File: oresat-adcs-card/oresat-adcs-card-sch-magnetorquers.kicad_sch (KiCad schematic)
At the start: 67 parts

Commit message: Design review changes
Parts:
- added R129: CRGCQ0603F2K7, oresat-acs-card:.0603-C-NOSILK, symbol oresat-acs-card-eagle-import:R-US_0603-C-NOSILK
- C17, C5, C53, C65, C66, C77: value (none) -> 10n; footprint (none) -> Capacitor_SMD:C_0603_1608Metric
- C18, C55, C67: value (none) -> 1n; footprint (none) -> Capacitor_SMD:C_0603_1608Metric
- C19, C56, C68: value (none) -> 22n; footprint (none) -> Capacitor_SMD:C_0603_1608Metric
- C26, C58, C70: value (none) -> 22u; footprint (none) -> Capacitor_SMD:C_0603_1608Metric
- C27, C40, C59, C61, C71, C73: value (none) -> NP; footprint (none) -> Capacitor_SMD:C_0603_1608Metric
- C41, C42, C62: value (none) -> 100n; footprint (none) -> Capacitor_SMD:C_0603_1608Metric
- C51, C54, C63: value (none) -> 4.7u; footprint (none) -> Capacitor_SMD:C_0603_1608Metric
- C52, C60, C72: value (none) -> 2.2u; footprint (none) -> Capacitor_SMD:C_0603_1608Metric
- R15, R16, R25: value (none) -> 30m; footprint (none) -> oresat-acs-card:WSK1206
- R17, R21, R23, R29: value (none) -> 1k; footprint (none) -> Resistor_SMD:R_0603_1608Metric
- R18, R24, R30: value (none) -> 47k; footprint (none) -> Resistor_SMD:R_0603_1608Metric
- R20: value (none) -> 100k; footprint (none) -> Resistor_SMD:R_0603_1608Metric
- R22: value (none) -> 18k; footprint (none) -> oresat-acs-card:.0603-C-NOSILK
- TP20, TP46, TP47, TP48, TP50, TP52, TP53, TP54, TP55, TP57, TP58, TP60, TP77, TP78, TP79, TP80, TP81, TP83, TP84: value (none) -> TEST-POINT-LARGE-SQUARE; footprint (none) -> oresat-acs-card:1X01
- U16, U22, U3: value (none) -> STSPIN250; footprint (none) -> Package_DFN_QFN:VQFN-16-1EP_3x3mm_P0.5mm_EP1.8x1.8mm
- U21, U23, U4: value (none) -> INA185; footprint (none) -> Package_TO_SOT_SMD:SOT-563
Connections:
- net GND: now also R129.1
- net MT_EN: now also R129.2
- net MT_REF: now reaches C5.1, C53.1, C65.1, R20.1, R21.2, TP20.1, U16.11 (REF), U22.11 (REF), U3.11 (REF)
- net MT_FAULT renamed MT_EN/~{FAULT}
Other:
- note added: "From MCU"
- note added: "MT_EN/~{FAULT}"
- note added: "STSPIN pulls EN/~{FAULT} low during failure disabling the magnetorquers"
- note added: "using 100x gain amp max 1 A out 1A*Rsense*100 = 3.0 V => 30 mΩ 30 mW"
- note removed: "30 mW max"
- note removed: "using 100x gain amp max 1 A out 1A*Rsense*100 = 3.0 V => 30 mΩ"
- moved on the sheet: C17, C18, C19, C26, C27, C40, C41, C5, C51, C52, R15, R17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

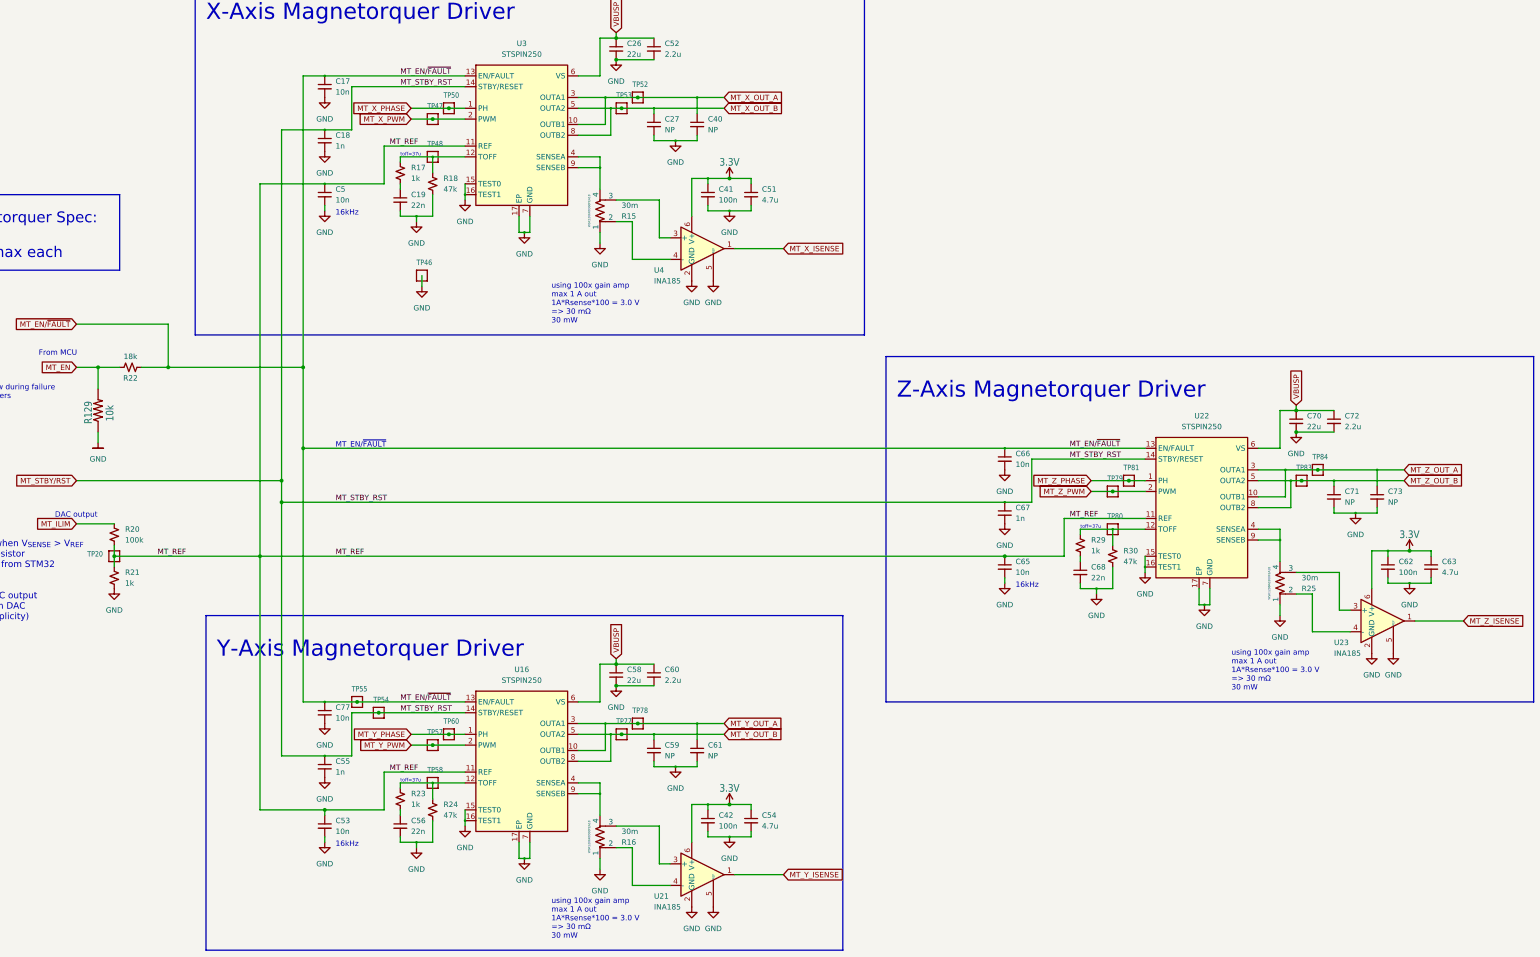
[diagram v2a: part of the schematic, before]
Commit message: Fixed ADCS card issues
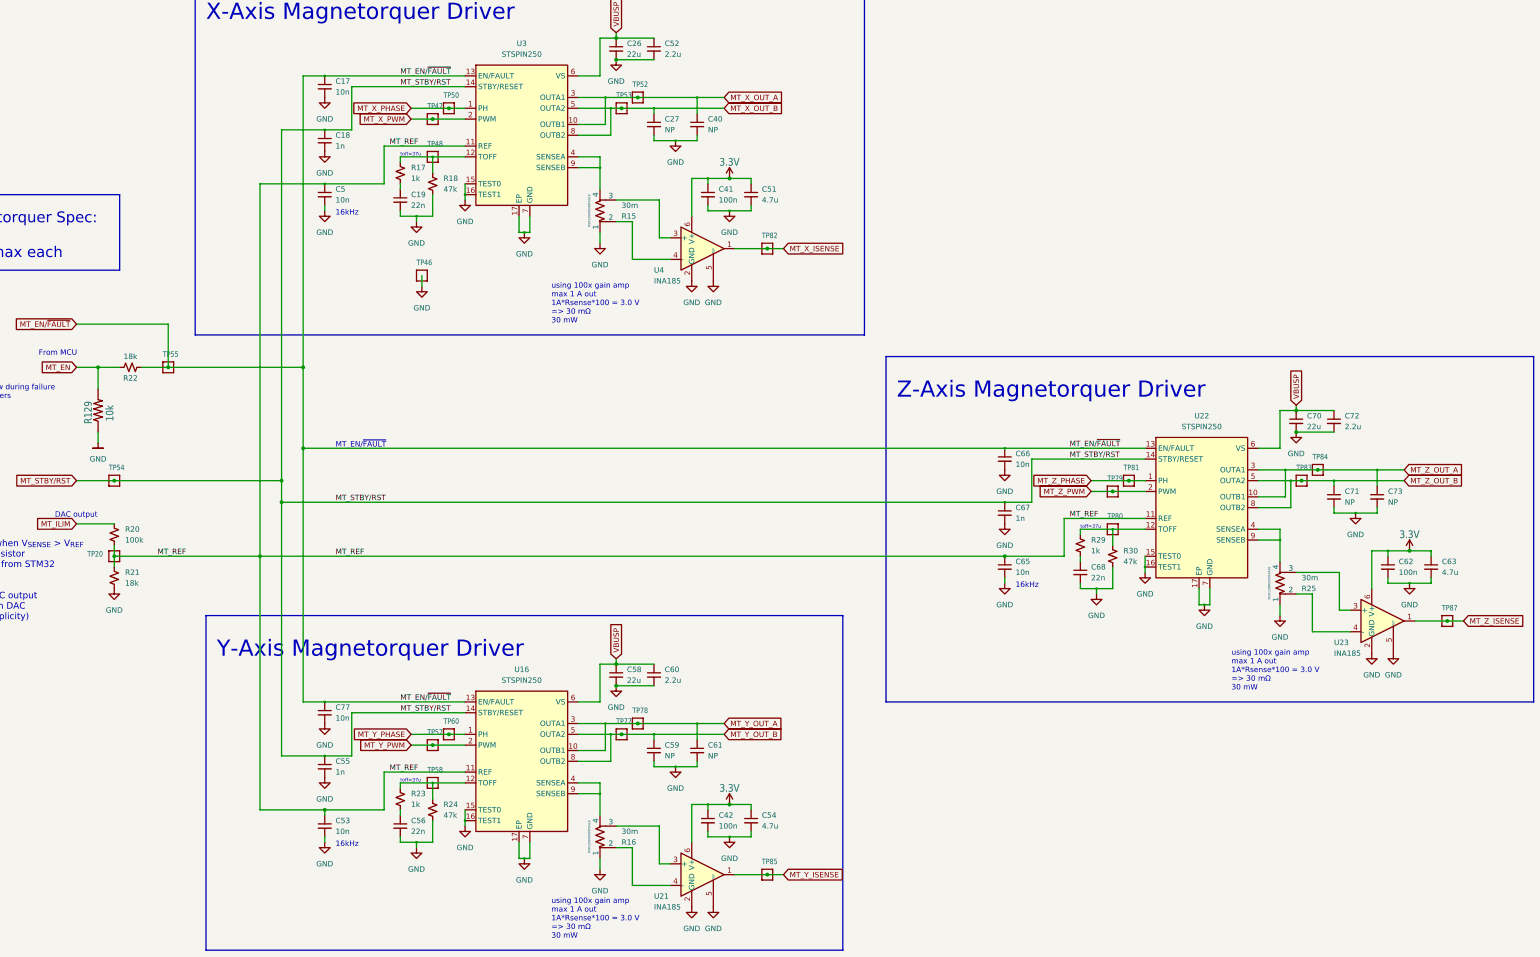
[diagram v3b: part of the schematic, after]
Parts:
- added TP82, TP85, TP87: TEST-POINT-LARGE-SQUARE, oresat-acs-card:1X01, symbol oresat-acs-card-eagle-import:TEST-POINT-LARGE-SQUARE
- R21: value 1k -> 18k
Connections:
- net MT_X_ISENSE: now also TP82.1
- net MT_Y_ISENSE: now also TP85.1
- net MT_Z_ISENSE: now also TP87.1
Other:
- moved on the sheet: TP54, TP55

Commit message: Fixed more ADCS card issues
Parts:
- added C100, C101, C102: 4.7u, Capacitor_SMD:C_0603_1608Metric, symbol Device:C_Small
- added R130, R131, R132: 1k, Resistor_SMD:R_0603_1608Metric, symbol Device:R_Small_US
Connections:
- net GND: now also C100.2, C101.2, C102.2
- net MT_X_ISENSE: now also C100.1, R130.2; no longer U4.1
- net MT_Y_ISENSE: now also C101.1, R131.2; no longer U21.1
- net MT_Z_ISENSE: now also C102.1, R132.2; no longer U23.1
- new net: R130.1, U4.1
- new net: R131.1, U21.1
- new net: R132.1, U23.1
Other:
- moved on the sheet: TP82, TP85, TP87

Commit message: Changed MT current limit setting, and added filter for current sense to ADC
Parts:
- added R133, R134, R135: 30m, Resistor_SMD:R_1206_3216Metric, symbol Device:R_Small_US
- C100, C101, C102: value 4.7u -> 100n
- R130, R131, R132: value 1k -> 10k
- R15, R16, R25: footprint oresat-acs-card:WSK1206 -> Resistor_SMD:R_1206_3216Metric; symbol Device:R_Shunt_US -> Device:R_Small_US; P/N WSK1206R0300FEA18 -> (none)
- R20: value 100k -> 23.7k
- R21: value 18k -> 1k
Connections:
- net GND: now also R133.1, R134.1, R135.1; no longer R15.1, R16.1, R25.1
- net at U4.3 (+): now also R15.2, U3.4 (SENSEA), U3.9 (SENSEB); no longer R15.3
- net at U4.4 (-): now also R15.1, R133.2; no longer R15.2
- net at U23.4 (-): now also R25.1, R135.2; no longer R25.2
- net at U23.3 (+): now also R25.2, U22.4 (SENSEA), U22.9 (SENSEB); no longer R25.3
- net at U21.4 (-): now also R16.1, R134.2; no longer R16.2
- net at U21.3 (+): now also R16.2, U16.4 (SENSEA), U16.9 (SENSEB); no longer R16.3
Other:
- note added: "50x gain amp"
- note added: "STSPIN current limits when V_{SENSE} > V_{REF} With 3.0 V out from DAC, V_{REF} = 0.12 V Sense resistor gives 60 mV/A, so max current limit is about 2 A"
- note removed: "STSPIN current limits when V_{SENSE} > V_{REF} 30 mV/A from sense resistor 0-3v0 (w/ intbuf) input from STM32 For 1 A max ctrl need 30 mV V_{REF} or 1/100 divider on DAC output results in 0.33 A/V from DAC (actually 1/101 for simplicity)"
- note removed: "using 100x gain amp max 1 A out 1A*Rsense*100 = 3.0 V => 30 mΩ 30 mW"

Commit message: Updated ADCS card and fixed library issues
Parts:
- R129, R22: footprint oresat-acs-card:.0603-C-NOSILK -> oresat-passives:0603-C-NOSILK
- U16, U22, U3: symbol U-STMicro-STSPIN250:STSPIN250 -> oresat-ics:STSPIN250
- U21, U23, U4: symbol U-TI-INA185-current-sense-amplifier:INA185 -> oresat-ics:INA185
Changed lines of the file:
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@@
     )
   )
-  (symbol (lib_id "U-TI-INA185-current-sense-amplifier:INA185") (at 203.2 83.82 0) (unit 1)
+  (symbol (lib_id "oresat-ics:INA185") (at 203.2 83.82 0) (unit 1)
     (in_bom yes) (on_board yes) (dnp no)
     (property "Reference" "U4" (at 191.77 88.8999 0)
@@
       (effects (font (size 1.778 1.5113)) (justify left bottom))
     )
-    (property "Footprint" "oresat-acs-card:.0603-C-NOSILK" (at 60.96 121.92 0)
+    (property "Footprint" "oresat-passives:0603-C-NOSILK" (at 60.96 121.92 0)
       (effects (font (size 1.27 1.27)) hide)
     )
@@
       (effects (font (size 1.27 1.27)))
     )
-    (property "Footprint" "oresat-acs-card:.0603-C-NOSILK" (at 68.58 111.76 0)
+    (property "Footprint" "oresat-passives:0603-C-NOSILK" (at 68.58 111.76 0)
       (effects (font (size 1.27 1.27)) hide)
     )
@@
     )
   )
-  (symbol (lib_id "U-STMicro-STSPIN250:STSPIN250") (at 321.31 133.35 0) (unit 1)
+  (symbol (lib_id "oresat-ics:STSPIN250") (at 321.31 133.35 0) (unit 1)
     (in_bom yes) (on_board yes) (dnp no) (fields_autoplaced)
     (property "Reference" "U22" (at 320.675 123.19 0)
@@
     )
   )
-  (symbol (lib_id "U-TI-INA185-current-sense-amplifier:INA185") (at 363.22 171.45 0) (unit 1)
+  (symbol (lib_id "oresat-ics:INA185") (at 363.22 171.45 0) (unit 1)
     (in_bom yes) (on_board yes) (dnp no)
     (property "Reference" "U23" (at 351.79 176.5299 0)
@@
     )
   )
-  (symbol (lib_name "STSPIN250_2") (lib_id "U-STMicro-STSPIN250:STSPIN250") (at 161.29 45.72 0) (unit 1)
+  (symbol (lib_id "oresat-ics:STSPIN250") (at 161.29 45.72 0) (unit 1)
     (in_bom yes) (on_board yes) (dnp no) (fields_autoplaced)
     (property "Reference" "U3" (at 160.655 35.56 0)
@@
     )
   )
-  (symbol (lib_id "OreSat-Power:GND") (at 60.96 129.54 0) (unit 1)
+  (symbol (lib_id "oresat-power:GND") (at 60.96 129.54 0) (unit 1)
     (in_bom yes) (on_board yes) (dnp no) (fields_autoplaced)
     (property "Reference" "#GND0150" (at 60.96 135.89 0)
@@
     )
   )
-  (symbol (lib_name "STSPIN250_1") (lib_id "U-STMicro-STSPIN250:STSPIN250") (at 161.29 193.04 0) (unit 1)
+  (symbol (lib_id "oresat-ics:STSPIN250") (at 161.29 193.04 0) (unit 1)
     (in_bom yes) (on_board yes) (dnp no) (fields_autoplaced)
     (property "Reference" "U16" (at 160.655 182.88 0)
@@
     )
   )
-  (symbol (lib_id "U-TI-INA185-current-sense-amplifier:INA185") (at 203.2 231.14 0) (unit 1)
+  (symbol (lib_id "oresat-ics:INA185") (at 203.2 231.14 0) (unit 1)
     (in_bom yes) (on_board yes) (dnp no)
     (property "Reference" "U21" (at 191.77 236.2199 0)

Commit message: Design review changes
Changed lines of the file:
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@@
     (effects (font (size 1.27 1.27)) (justify left))
     (property "Intersheetrefs" "${INTERSHEET_REFS}" (at 182.8006 24.4383 90)
-      (effects (font (size 1.27 1.27)) (justify left) hide)
+      (effects (font (size 1.27 1.27)) (justify left))
     )
   )
-  (global_label "MT_Z_ISENSE" (shape input) (at 384.81 171.45 0) (fields_autoplaced)
+  (global_label "MT_Z_ISENSE" (shape output) (at 384.81 171.45 0) (fields_autoplaced)
     (effects (font (size 1.27 1.27)) (justify left))
-    (property "Intersheetrefs" "${INTERSHEET_REFS}" (at 399.8626 171.3706 0)
-      (effects (font (size 1.27 1.27)) (justify left) hide)
+    (property "Intersheetrefs" "${INTERSHEET_REFS}" (at 399.9318 171.45 0)
+      (effects (font (size 1.27 1.27)) (justify left))
     )
   )
@@
     (effects (font (size 1.27 1.27)) (justify right))
     (property "Intersheetrefs" "${INTERSHEET_REFS}" (at 280.1921 138.3506 0)
-      (effects (font (size 1.27 1.27)) (justify right) hide)
+      (effects (font (size 1.27 1.27)) (justify right))
     )
   )
-  (global_label "MT_X_OUT_A" (shape input) (at 208.28 48.26 0) (fields_autoplaced)
+  (global_label "MT_X_OUT_A" (shape output) (at 208.28 48.26 0) (fields_autoplaced)
     (effects (font (size 1.27 1.27)) (justify left))
-    (property "Intersheetrefs" "${INTERSHEET_REFS}" (at 222.365 48.1806 0)
-      (effects (font (size 1.27 1.27)) (justify left) hide)
+    (property "Intersheetrefs" "${INTERSHEET_REFS}" (at 222.4343 48.26 0)
+      (effects (font (size 1.27 1.27)) (justify left))
     )
   )
@@
     (effects (font (size 1.27 1.27)) (justify left))
     (property "Intersheetrefs" "${INTERSHEET_REFS}" (at 182.8006 171.7583 90)
-      (effects (font (size 1.27 1.27)) (justify left) hide)
+      (effects (font (size 1.27 1.27)) (justify left))
     )
   )
@@
     (effects (font (size 1.27 1.27)) (justify right))
     (property "Intersheetrefs" "${INTERSHEET_REFS}" (at 122.1679 200.5806 0)
-      (effects (font (size 1.27 1.27)) (justify right) hide)
+      (effects (font (size 1.27 1.27)) (justify right))
     )
   )
@@
     (effects (font (size 1.27 1.27)) (justify right))
     (property "Intersheetrefs" "${INTERSHEET_REFS}" (at 120.1721 50.7206 0)
-      (effects (font (size 1.27 1.27)) (justify right) hide)
+      (effects (font (size 1.27 1.27)) (justify right))
     )
   )
   (global_label "MT_ILIM" (shape input) (at 55.88 148.59 180) (fields_autoplaced)
     (effects (font (size 1.27 1.27)) (justify right))
-    (property "Intersheetrefs" "${INTERSHEET_REFS}" (at 33.8726 148.5106 0)
-      (effects (font (size 1.27 1.27)) (justify right) hide)
+    (property "Intersheetrefs" "${INTERSHEET_REFS}" (at 45.8985 148.59 0)
+      (effects (font (size 1.27 1.27)) (justify right))
     )
   )
-  (global_label "MT_Y_OUT_A" (shape input) (at 208.28 195.58 0) (fields_autoplaced)
+  (global_label "MT_Y_OUT_A" (shape output) (at 208.28 195.58 0) (fields_autoplaced)
     (effects (font (size 1.27 1.27)) (justify left))
-    (property "Intersheetrefs" "${INTERSHEET_REFS}" (at 221.8207 195.5006 0)
-      (effects (font (size 1.27 1.27)) (justify left) hide)
+    (property "Intersheetrefs" "${INTERSHEET_REFS}" (at 222.3134 195.58 0)
+      (effects (font (size 1.27 1.27)) (justify left))
     )
   )
@@
     (effects (font (size 1.27 1.27)) (justify right))
     (property "Intersheetrefs" "${INTERSHEET_REFS}" (at 120.2931 198.0406 0)
-      (effects (font (size 1.27 1.27)) (justify right) hide)
+      (effects (font (size 1.27 1.27)) (justify right))
     )
   )
-  (global_label "MT_X_OUT_B" (shape input) (at 208.28 50.8 0) (fields_autoplaced)
+  (global_label "MT_X_OUT_B" (shape output) (at 208.28 50.8 0) (fields_autoplaced)
     (effects (font (size 1.27 1.27)) (justify left))
-    (property "Intersheetrefs" "${INTERSHEET_REFS}" (at 222.5464 50.7206 0)
-      (effects (font (size 1.27 1.27)) (justify left) hide)
+    (property "Intersheetrefs" "${INTERSHEET_REFS}" (at 222.6157 50.8 0)
+      (effects (font (size 1.27 1.27)) (justify left))
     )
   )
-  (global_label "MT_Y_OUT_B" (shape input) (at 208.28 198.12 0) (fields_autoplaced)
+  (global_label "MT_Y_OUT_B" (shape output) (at 208.28 198.12 0) (fields_autoplaced)
     (effects (font (size 1.27 1.27)) (justify left))
-    (property "Intersheetrefs" "${INTERSHEET_REFS}" (at 222.0021 198.0406 0)
-      (effects (font (size 1.27 1.27)) (justify left) hide)
+    (property "Intersheetrefs" "${INTERSHEET_REFS}" (at 222.4948 198.12 0)
+      (effects (font (size 1.27 1.27)) (justify left))
     )
   )
@@
     (effects (font (size 1.27 1.27)) (justify left))
     (property "Intersheetrefs" "${INTERSHEET_REFS}" (at 342.8206 112.0683 90)
-      (effects (font (size 1.27 1.27)) (justify left) hide)
+      (effects (font (size 1.27 1.27)) (justify left))
     )
   )
   (global_label "MT_STBY{slash}RST" (shape input) (at 55.88 138.43 180) (fields_autoplaced)
     (effects (font (size 1.27 1.27)) (justify right))
-    (property "Intersheetrefs" "${INTERSHEET_REFS}" (at 40.7669 138.3506 0)
-      (effects (font (size 1.27 1.27)) (justify right) hide)
+    (property "Intersheetrefs" "${INTERSHEET_REFS}" (at 40.2743 138.43 0)
+      (effects (font (size 1.27 1.27)) (justify right))
     )
   )
-  (global_label "MT_EN{slash}~{FAULT}" (shape input) (at 55.88 101.6 180) (fields_autoplaced)
+  (global_label "MT_EN{slash}~{FAULT}" (shape output) (at 55.88 101.6 180) (fields_autoplaced)
     (effects (font (size 1.27 1.27)) (justify right))
-    (property "Intersheetrefs" "${INTERSHEET_REFS}" (at 40.7669 101.6794 0)
-      (effects (font (size 1.27 1.27)) (justify right) hide)
+    (property "Intersheetrefs" "${INTERSHEET_REFS}" (at 40.2742 101.6 0)
+      (effects (font (size 1.27 1.27)) (justify right))
     )
   )
-  (global_label "MT_Z_OUT_A" (shape input) (at 368.3 135.89 0) (fields_autoplaced)
+  (global_label "MT_Z_OUT_A" (shape output) (at 368.3 135.89 0) (fields_autoplaced)
     (effects (font (size 1.27 1.27)) (justify left))
-    (property "Intersheetrefs" "${INTERSHEET_REFS}" (at 382.385 135.8106 0)
-      (effects (font (size 1.27 1.27)) (justify left) hide)
+    (property "Intersheetrefs" "${INTERSHEET_REFS}" (at 382.4543 135.89 0)
+      (effects (font (size 1.27 1.27)) (justify left))
     )
   )
   (global_label "MT_EN" (shape input) (at 55.88 111.76 180) (fields_autoplaced)
     (effects (font (size 1.27 1.27)) (justify right))
-    (property "Intersheetrefs" "${INTERSHEET_REFS}" (at 35.0821 111.6806 0)
-      (effects (font (size 1.27 1.27)) (justify right) hide)
+    (property "Intersheetrefs" "${INTERSHEET_REFS}" (at 47.1081 111.76 0)
+      (effects (font (size 1.27 1.27)) (justify right))
     )
   )
-  (global_label "MT_X_ISENSE" (shape input) (at 224.79 83.82 0) (fields_autoplaced)
+  (global_label "MT_X_ISENSE" (shape output) (at 224.79 83.82 0) (fields_autoplaced)
     (effects (font (size 1.27 1.27)) (justify left))
-    (property "Intersheetrefs" "${INTERSHEET_REFS}" (at 239.8426 83.7406 0)
-      (effects (font (size 1.27 1.27)) (justify left) hide)
+    (property "Intersheetrefs" "${INTERSHEET_REFS}" (at 239.9118 83.82 0)
+      (effects (font (size 1.27 1.27)) (justify left))
     )
   )
@@
     (effects (font (size 1.27 1.27)) (justify right))
     (property "Intersheetrefs" "${INTERSHEET_REFS}" (at 282.0669 140.8906 0)
-      (effects (font (size 1.27 1.27)) (justify right) hide)
+      (effects (font (size 1.27 1.27)) (justify right))
     )
   )
-  (global_label "MT_Y_ISENSE" (shape input) (at 223.52 231.14 0) (fields_autoplaced)
+  (global_label "MT_Y_ISENSE" (shape output) (at 223.52 231.14 0) (fields_autoplaced)
     (effects (font (size 1.27 1.27)) (justify left))
-    (property "Intersheetrefs" "${INTERSHEET_REFS}" (at 238.0283 231.0606 0)
-      (effects (font (size 1.27 1.27)) (justify left) hide)
+    (property "Intersheetrefs" "${INTERSHEET_REFS}" (at 238.5209 231.14 0)
+      (effects (font (size 1.27 1.27)) (justify left))
     )
   )
@@
     (effects (font (size 1.27 1.27)) (justify right))
     (property "Intersheetrefs" "${INTERSHEET_REFS}" (at 122.0469 53.2606 0)
-      (effects (font (size 1.27 1.27)) (justify right) hide)
+      (effects (font (size 1.27 1.27)) (justify right))
     )
   )
-  (global_label "MT_Z_OUT_B" (shape input) (at 368.3 138.43 0) (fields_autoplaced)
+  (global_label "MT_Z_OUT_B" (shape output) (at 368.3 138.43 0) (fields_autoplaced)
     (effects (font (size 1.27 1.27)) (justify left))
-    (property "Intersheetrefs" "${INTERSHEET_REFS}" (at 382.5664 138.3506 0)
-      (effects (font (size 1.27 1.27)) (justify left) hide)
+    (property "Intersheetrefs" "${INTERSHEET_REFS}" (at 382.6357 138.43 0)
+      (effects (font (size 1.27 1.27)) (justify left))
     )
   )
